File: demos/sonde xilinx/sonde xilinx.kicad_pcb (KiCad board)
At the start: 2 copper layers, 29 parts, among them J1 DB25MALE, J2 DB9MALE, P1 CONN_6, U1 74LS125, U2 74LS125

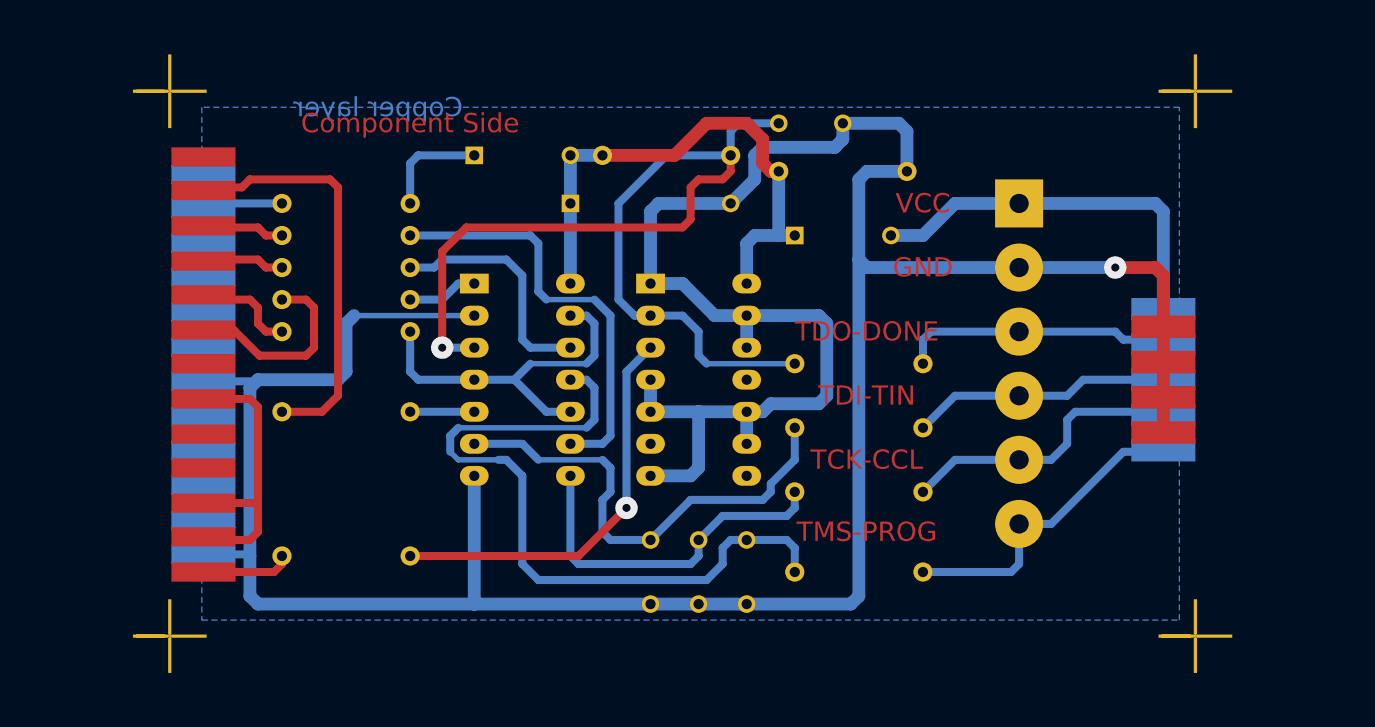
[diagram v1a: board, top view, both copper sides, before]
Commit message: Update demos. Fix  pspice netlist issues when using ( and ) in net names ( parenthesis are replaced by underscore) .
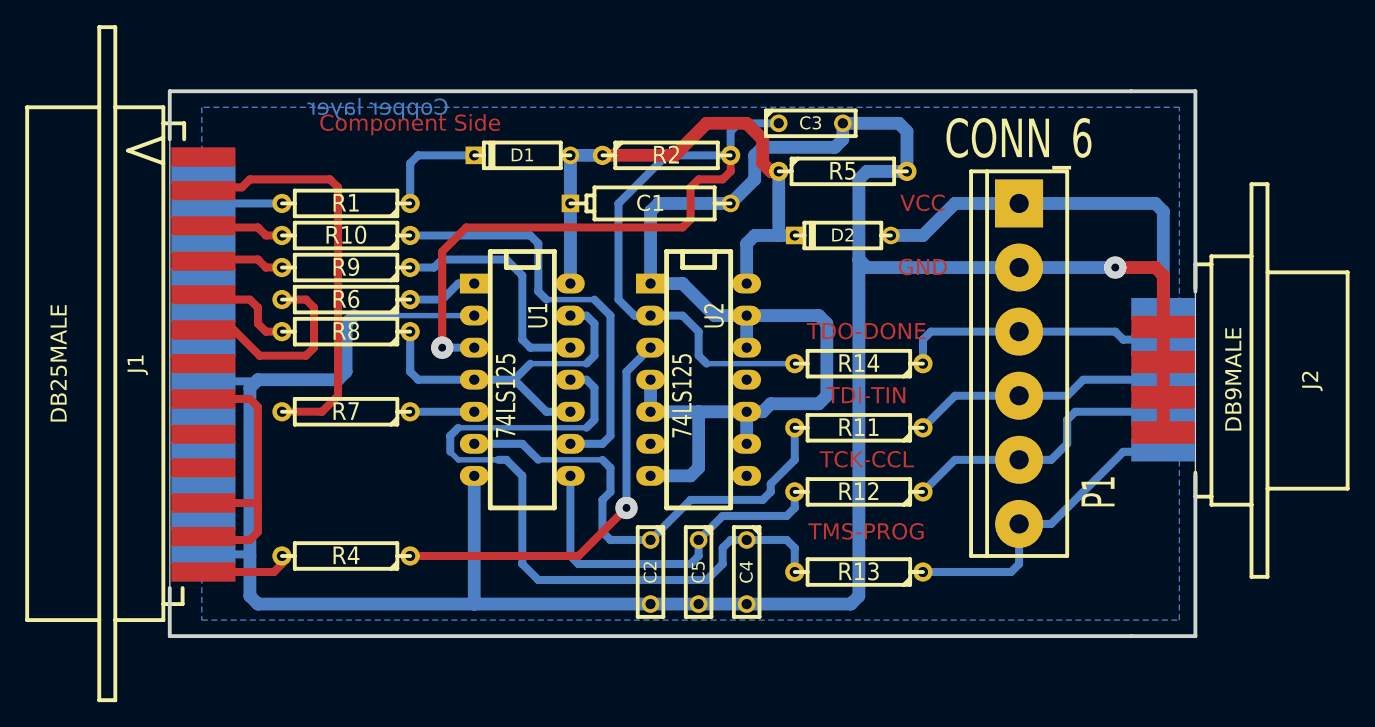
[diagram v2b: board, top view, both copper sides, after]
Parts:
- removed MIRE (x4): *, MIRE
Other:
- board outline added: 81.3 x 43.2 mm
